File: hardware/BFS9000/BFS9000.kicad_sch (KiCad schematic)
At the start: 16 parts, among them J1 Conn_01x04, J2 MJ-4PP-9, J3 Conn_01x04, J4 Conn_01x04, Q1 Si2301CDS, U1 RP2040 Core board

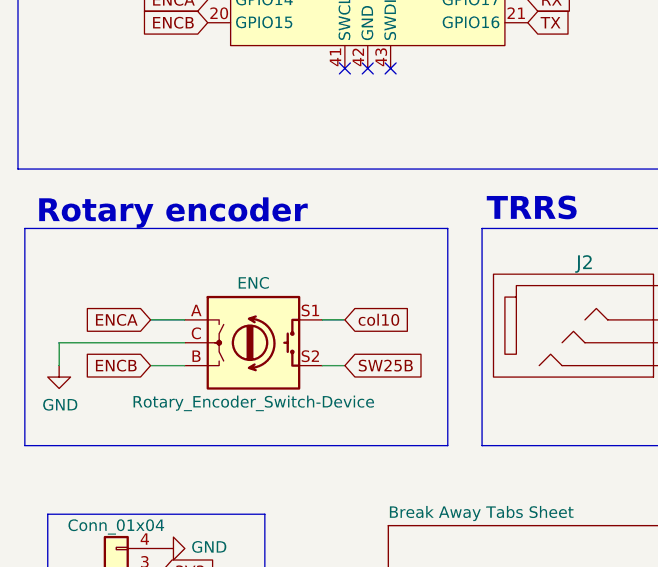
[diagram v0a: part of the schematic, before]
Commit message: feat(hardware): remove MULEDs and reconnect all orphaned traces
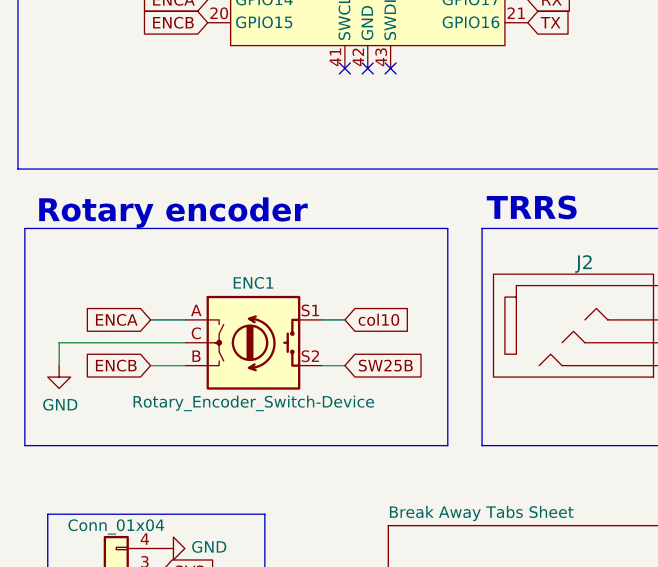
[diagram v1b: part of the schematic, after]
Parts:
- renumbered ENC to ENC1
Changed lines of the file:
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@@
 		(on_board yes)
 		(dnp no)
-		(property "Reference" "ENC"
+		(property "Reference" "ENC1"
 			(at 44.45 112.776 0)
 			(effects
@@
 			(project "Custom split ergonomic keyboard PCB"
 				(path "/df2b308e-7efe-4cc0-aa51-822cf3ef83df"
-					(reference "ENC")
+					(reference "ENC1")
 					(unit 1)
 				)
